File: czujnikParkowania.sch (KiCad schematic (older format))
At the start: 38 parts, among them J1 Screw_Terminal_01x03, Q1 BC817, Q2 IRF7404, Q3 BC817, Q4 BC817, Q5 BC817, U1 DC56-11SEKWA, U2 LM7805_TO220, U3 HC-SR04

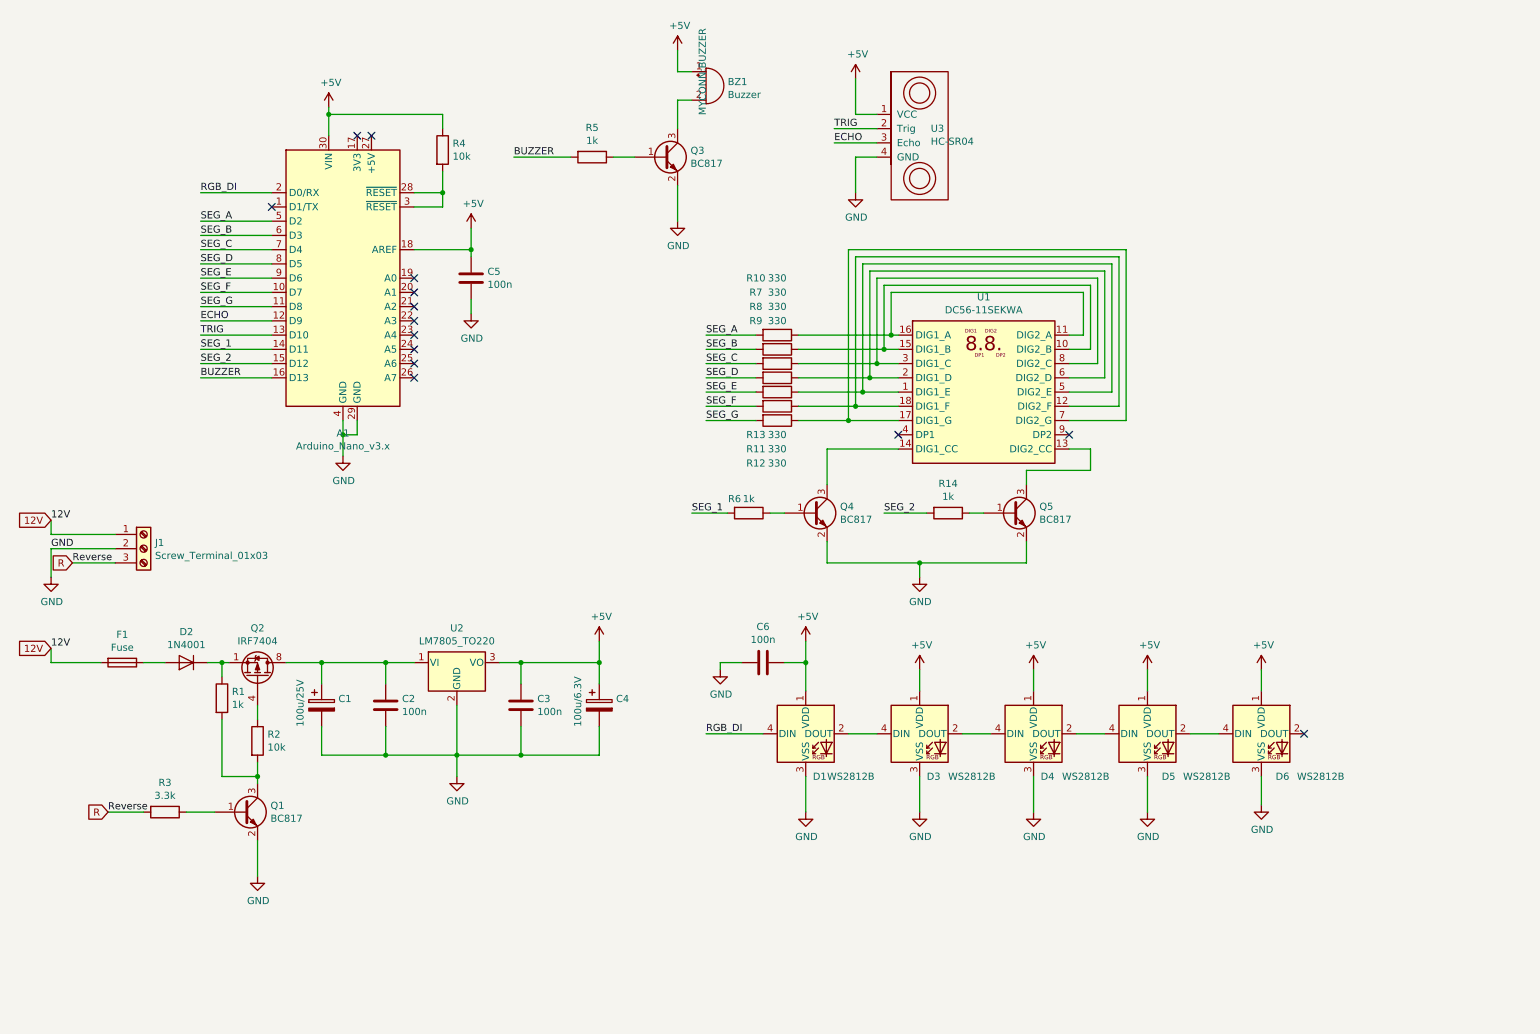
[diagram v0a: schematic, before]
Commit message: version with Amega only
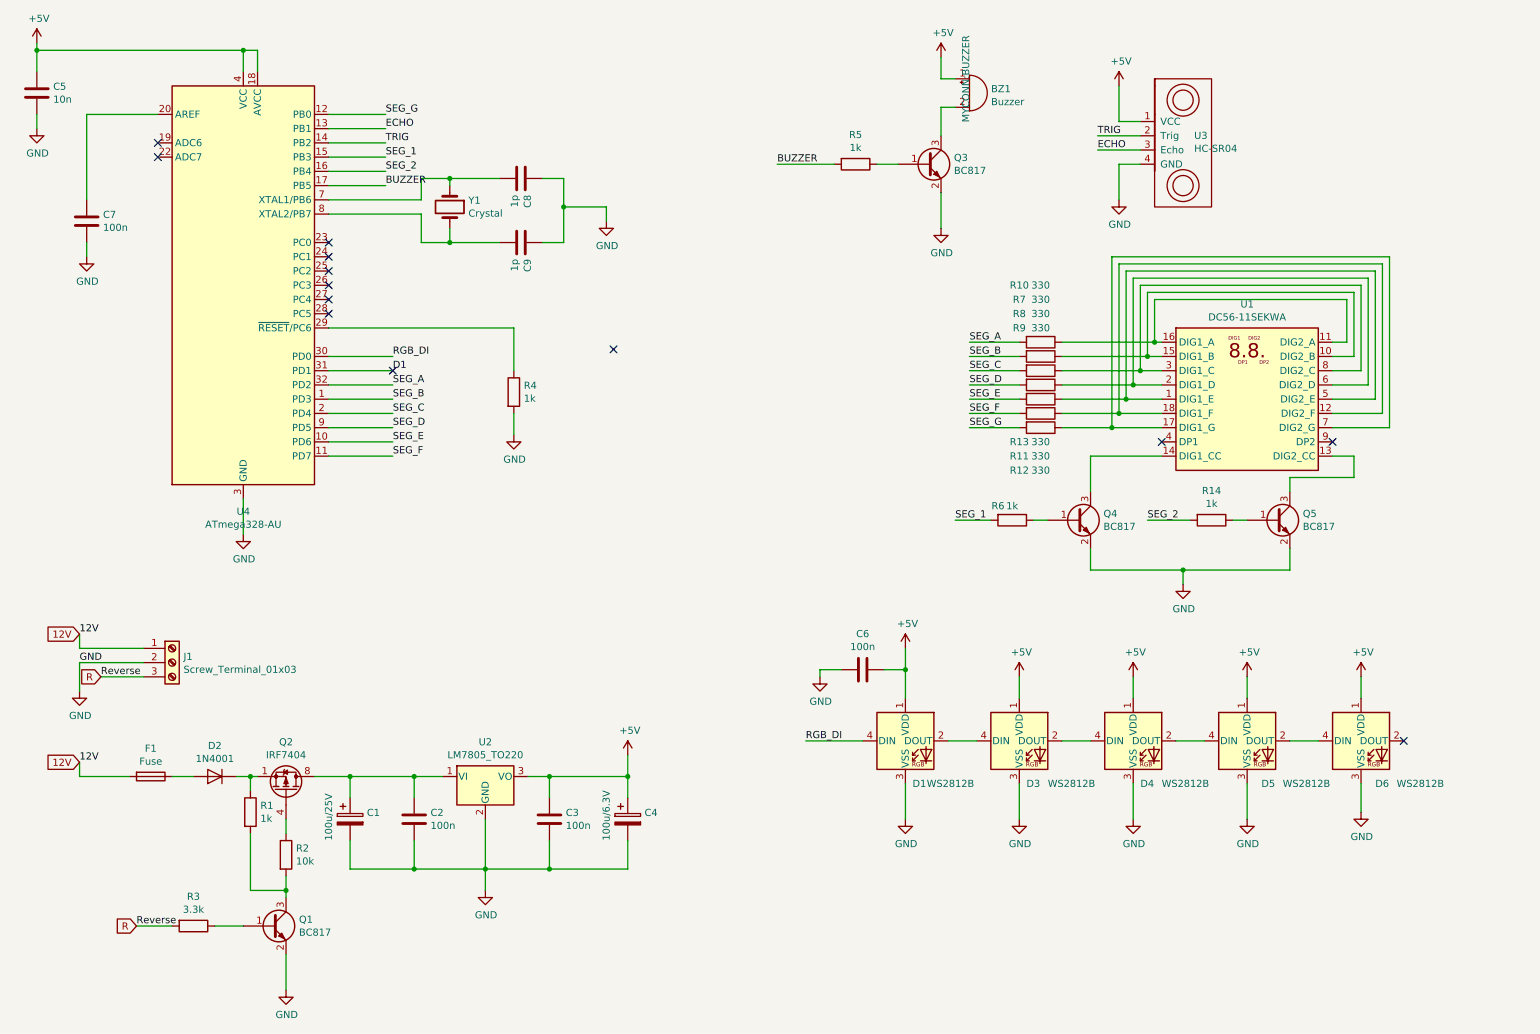
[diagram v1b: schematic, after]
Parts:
- removed A1: Arduino_Nano_v3.x, Module:Arduino_Nano, symbol MCU_Module:Arduino_Nano_v3.x
- added C7: 100n, Capacitor_SMD:C_0805_2012Metric, symbol Device:C
- added C8, C9: 1p, Capacitor_SMD:C_0805_2012Metric, symbol Device:C
- added U4: ATmega328-AU, Package_QFP:TQFP-32_7x7mm_P0.8mm, symbol MCU_Microchip_ATmega:ATmega328-AU
- added Y1: Crystal, MYCONN:16MHz cristal oscillator, symbol Device:Crystal
- C5: value 100n -> 10n
- R4: value 10k -> 1k
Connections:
- net +5V: now also U4.18 (AVCC), U4.4 (VCC), U4.6 (VCC); no longer R4.1
- net BUZZER: now also U4.17 (PB5)
- net ECHO: now also U4.13 (PB1)
- net GND: now also R4.2, C7.2, C8.1, C9.1, U4.21 (GND), U4.3 (GND), U4.5 (GND)
- net RGB_DI: now also U4.30 (PD0)
- net SEG_1: now also U4.15 (PB3)
- net SEG_2: now also U4.16 (PB4)
- net SEG_A: now also U4.32 (PD2)
- net SEG_B: now also U4.1 (PD3)
- net SEG_C: now also U4.2 (PD4)
- net SEG_D: now also U4.9 (PD5)
- net SEG_E: now also U4.10 (PD6)
- net SEG_F: now also U4.11 (PD7)
- net SEG_G: now also U4.12 (PB0)
- net TRIG: now also U4.14 (PB2)
- new net: C7.1, U4.20 (AREF)
- new net: R4.1, U4.29 (~RESET~/PC6)
- new net: C8.2, U4.7 (XTAL1/PB6), Y1.1
- new net: C9.2, U4.8 (XTAL2/PB7), Y1.2
- new net D1: U4.31 (PD1)
- no-connect marks 14 -> 13
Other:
- moved on the sheet: BZ1, C1, C2, C3, C4, C5, C6, D1, D2, D3, D4, D5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

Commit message: Adruino and Atmega328 on single board for code dev
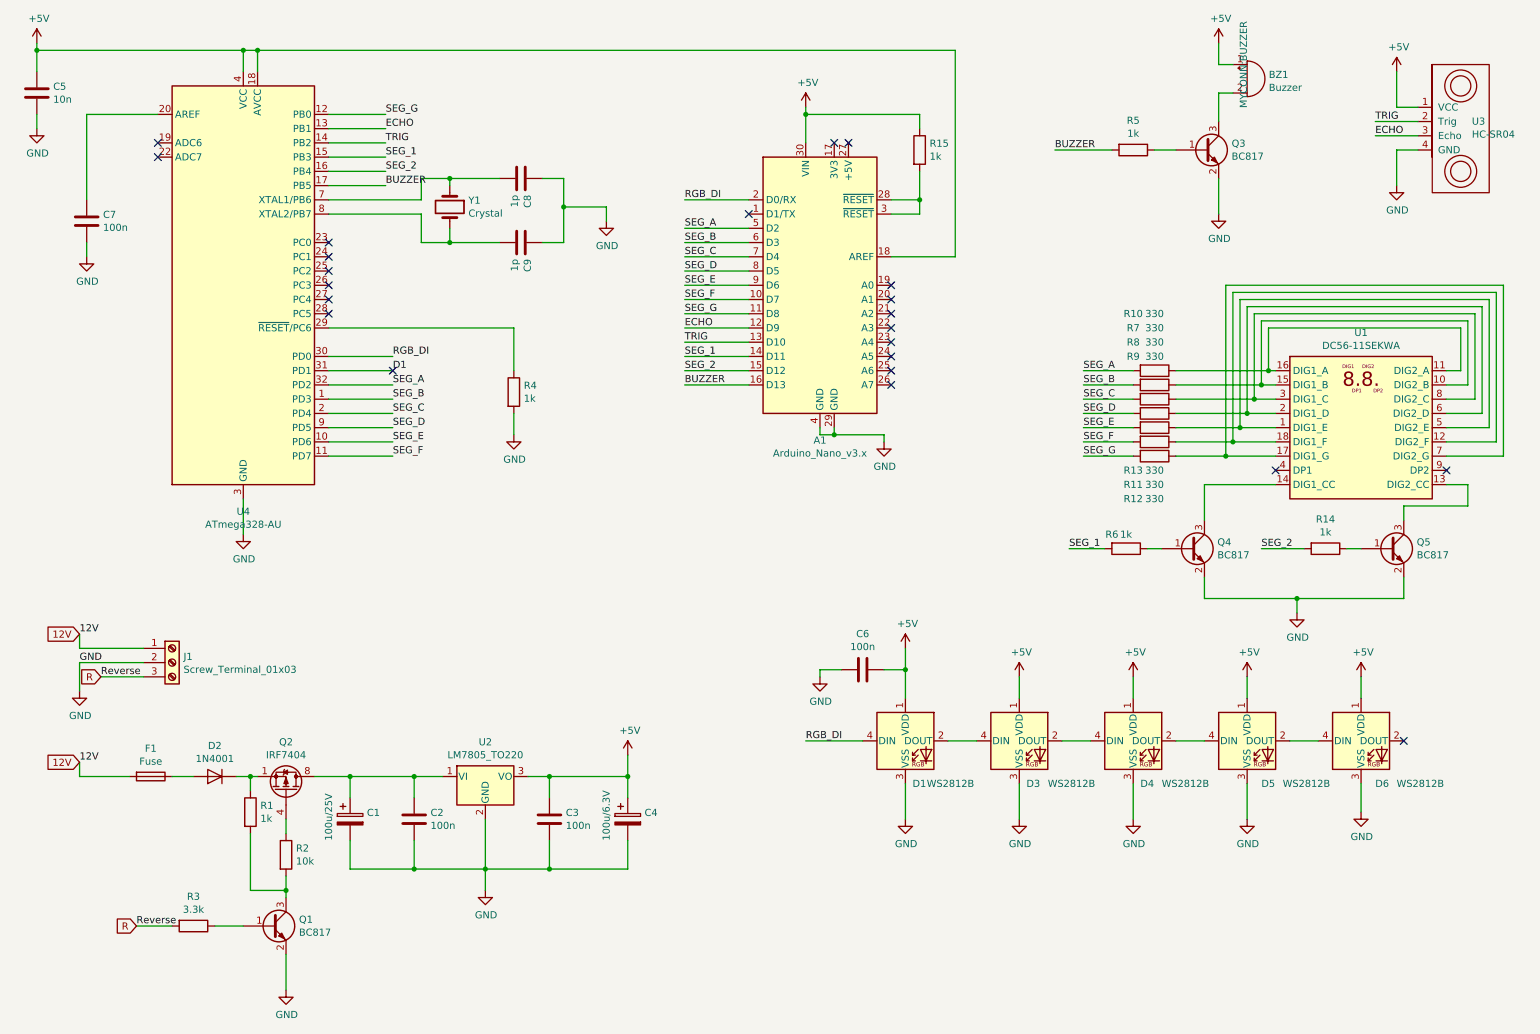
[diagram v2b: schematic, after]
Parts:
- added A1: Arduino_Nano_v3.x, Module:Arduino_Nano, symbol MCU_Module:Arduino_Nano_v3.x
- added R15: 1k, Resistor_SMD:R_0805_2012Metric, symbol Device:R
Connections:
- net +5V: now also A1.18 (AREF), A1.30 (VIN), R15.1
- net BUZZER: now also A1.16 (D13)
- net ECHO: now also A1.12 (D9)
- net GND: now also A1.29 (GND), A1.4 (GND)
- net RGB_DI: now also A1.2 (D0/RX)
- net SEG_1: now also A1.14 (D11)
- net SEG_2: now also A1.15 (D12)
- net SEG_A: now also A1.5 (D2)
- net SEG_B: now also A1.6 (D3)
- net SEG_C: now also A1.7 (D4)
- net SEG_D: now also A1.8 (D5)
- net SEG_E: now also A1.9 (D6)
- net SEG_F: now also A1.10 (D7)
- net SEG_G: now also A1.11 (D8)
- net TRIG: now also A1.13 (D10)
- new net: A1.28 (~RESET), A1.3 (~RESET), R15.2
- no-connect marks 13 -> 23
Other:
- moved on the sheet: BZ1, Q3, Q4, Q5, R10, R11, R12, R13, R14, R5, R6, R7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

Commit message: Added button
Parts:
- added SW?: SW_Push, symbol Switch:SW_Push
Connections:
- net D1 is gone; now on net BTN: U4.31 (PD1)
- net GND: now also SW?.2
- net BTN: now reaches A1.1 (D1/TX)
- net BTN: now also SW?.1
- no-connect marks 23 -> 21
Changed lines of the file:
@@
 RGB_DI
 Text Label 3150 3050 0    50   ~ 0
-D1
+BTN
 Text Label 3150 3150 0    50   ~ 0
 SEG_A
@@
 Text Label 3100 1750 0    50   ~ 0
 BUZZER
-NoConn ~ 3150 3050
 $Comp
 L MCU_Module:Arduino_Nano_v3.x A1
@@
 NoConn ~ 6650 3050
 NoConn ~ 6650 3150
-NoConn ~ 5650 1950
 $Comp
 L power:+5V #PWR0107
@@
 Text Label 5200 3150 0    50   ~ 0
 BUZZER
+$Comp
+L Switch:SW_Push SW?
+U 1 1 5EA69D05
+P 3700 4350
+F 0 "SW?" H 3700 4635 50  0000 C CNN
+F 1 "SW_Push" H 3700 4544 50  0000 C CNN
+F 2 "" H 3700 4550 50  0001 C CNN
+F 3 "~" H 3700 4550 50  0001 C CNN
+	1    3700 4350
+	1    0    0    -1
+$EndComp
+Wire Wire Line
+	5650 1950 5200 1950
+Text Label 5200 1950 0    50   ~ 0
+BTN
+Wire Wire Line
+	3500 4350 3150 4350
+$Comp
+L power:GND #PWR?
+U 1 1 5EAA1D9B
+P 4100 4450
+F 0 "#PWR?" H 4100 4200 50  0001 C CNN
+F 1 "GND" H 4105 4277 50  0000 C CNN
+F 2 "" H 4100 4450 50  0001 C CNN
+F 3 "" H 4100 4450 50  0001 C CNN
+	1    4100 4450
+	1    0    0    -1
+$EndComp
+Wire Wire Line
+	3900 4350 4100 4350
+Wire Wire Line
+	4100 4350 4100 4450
+Text Label 3150 4350 0    50   ~ 0
+BTN
 $EndSCHEMATC

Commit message: bug on schematic and missing connection on PCB
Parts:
- SW1: renamed from SW?; footprint (none) -> Button_Switch_SMD:SW_SPST_B3S-1000
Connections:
- net +5V: no longer A1.18 (AREF)
- net at C7.1, U4.20 (AREF): now also A1.18 (AREF)
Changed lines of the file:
@@
 	6650 2250 7100 2250
-Wire Wire Line
-	7100 2250 7100 800
-Wire Wire Line
-	7100 800  2200 800
-Connection ~ 2200 800
 Wire Wire Line
 	5650 1850 5200 1850
@@
 BUZZER
 $Comp
-L Switch:SW_Push SW?
+L Switch:SW_Push SW1
 U 1 1 5EA69D05
 P 3700 4350
-F 0 "SW?" H 3700 4635 50  0000 C CNN
+F 0 "SW1" H 3700 4635 50  0000 C CNN
 F 1 "SW_Push" H 3700 4544 50  0000 C CNN
-F 2 "" H 3700 4550 50  0001 C CNN
-F 3 "~" H 3700 4550 50  0001 C CNN
+F 2 "Button_Switch_SMD:SW_SPST_B3S-1000" H 3700 4550 50  0001 C CNN
+F 3 "https://www.tme.eu/pl/details/b3s-1000/mikroprzelaczniki-tact/omron-ocb/" H 3700 4550 50  0001 C CNN
 	1    3700 4350
 	1    0    0    -1
@@
 	3500 4350 3150 4350
 $Comp
-L power:GND #PWR?
+L power:GND #PWR0129
 U 1 1 5EAA1D9B
 P 4100 4450
-F 0 "#PWR?" H 4100 4200 50  0001 C CNN
+F 0 "#PWR0129" H 4100 4200 50  0001 C CNN
 F 1 "GND" H 4105 4277 50  0000 C CNN
 F 2 "" H 4100 4450 50  0001 C CNN
@@
 Text Label 3150 4350 0    50   ~ 0
 BTN
+Wire Wire Line
+	7100 650  1000 650
+Wire Wire Line
+	1000 650  1000 1250
+Wire Wire Line
+	7100 650  7100 2250
+Connection ~ 1000 1250
 $EndSCHEMATC

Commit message: added capacitors
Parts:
- added C10, C11, C12, C13: 100n, Capacitor_SMD:C_0805_2012Metric, symbol Device:C
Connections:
- net +5V: now also C10.1, C11.1, C12.1, C13.1
- net GND: now also C10.2, C11.2, C12.2, C13.2
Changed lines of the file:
@@
 L power:+5V #PWR0121
 U 1 1 5EB28EBD
-P 7550 5200
-F 0 "#PWR0121" H 7550 5050 50  0001 C CNN
-F 1 "+5V" H 7565 5373 50  0000 C CNN
-F 2 "" H 7550 5200 50  0001 C CNN
-F 3 "" H 7550 5200 50  0001 C CNN
-	1    7550 5200
+P 7550 5000
+F 0 "#PWR0121" H 7550 4850 50  0001 C CNN
+F 1 "+5V" H 7565 5173 50  0000 C CNN
+F 2 "" H 7550 5000 50  0001 C CNN
+F 3 "" H 7550 5000 50  0001 C CNN
+	1    7550 5000
 	1    0    0    -1
 $EndComp
@@
 L power:+5V #PWR0122
 U 1 1 5EB296B5
-P 8350 5200
-F 0 "#PWR0122" H 8350 5050 50  0001 C CNN
-F 1 "+5V" H 8365 5373 50  0000 C CNN
-F 2 "" H 8350 5200 50  0001 C CNN
-F 3 "" H 8350 5200 50  0001 C CNN
-	1    8350 5200
+P 8350 5000
+F 0 "#PWR0122" H 8350 4850 50  0001 C CNN
+F 1 "+5V" H 8365 5173 50  0000 C CNN
+F 2 "" H 8350 5000 50  0001 C CNN
+F 3 "" H 8350 5000 50  0001 C CNN
+	1    8350 5000
 	1    0    0    -1
 $EndComp
@@
 L power:+5V #PWR0123
 U 1 1 5EB2995A
-P 9150 5200
-F 0 "#PWR0123" H 9150 5050 50  0001 C CNN
-F 1 "+5V" H 9165 5373 50  0000 C CNN
-F 2 "" H 9150 5200 50  0001 C CNN
-F 3 "" H 9150 5200 50  0001 C CNN
-	1    9150 5200
+P 9150 5000
+F 0 "#PWR0123" H 9150 4850 50  0001 C CNN
+F 1 "+5V" H 9165 5173 50  0000 C CNN
+F 2 "" H 9150 5000 50  0001 C CNN
+F 3 "" H 9150 5000 50  0001 C CNN
+	1    9150 5000
 	1    0    0    -1
 $EndComp
@@
 L power:+5V #PWR0124
 U 1 1 5EB29CCE
-P 9950 5200
-F 0 "#PWR0124" H 9950 5050 50  0001 C CNN
-F 1 "+5V" H 9965 5373 50  0000 C CNN
-F 2 "" H 9950 5200 50  0001 C CNN
-F 3 "" H 9950 5200 50  0001 C CNN
-	1    9950 5200
-	1    0    0    -1
-$EndComp
-Wire Wire Line
-	7550 5200 7550 5350
-Wire Wire Line
-	8350 5200 8350 5350
-Wire Wire Line
-	9150 5200 9150 5350
-Wire Wire Line
-	9950 5200 9950 5350
+P 9950 5000
+F 0 "#PWR0124" H 9950 4850 50  0001 C CNN
+F 1 "+5V" H 9965 5173 50  0000 C CNN
+F 2 "" H 9950 5000 50  0001 C CNN
+F 3 "" H 9950 5000 50  0001 C CNN
+	1    9950 5000
+	1    0    0    -1
+$EndComp
 Wire Wire Line
 	7050 5650 7250 5650
@@
 	7100 650  7100 2250
 Connection ~ 1000 1250
+Wire Wire Line
+	9950 5000 9950 5150
+Wire Wire Line
+	9150 5000 9150 5150
+Wire Wire Line
+	8350 5000 8350 5150
+Wire Wire Line
+	7550 5000 7550 5150
+$Comp
+L Device:C C10
+U 1 1 5EC7958F
+P 7250 5150
+F 0 "C10" V 6998 5150 50  0000 C CNN
+F 1 "100n" V 7089 5150 50  0000 C CNN
+F 2 "Capacitor_SMD:C_0805_2012Metric" H 7288 5000 50  0001 C CNN
+F 3 "~" H 7250 5150 50  0001 C CNN
+	1    7250 5150
+	0    1    1    0
+$EndComp
+$Comp
+L Device:C C11
+U 1 1 5EC79A1F
+P 8050 5150
+F 0 "C11" V 7798 5150 50  0000 C CNN
+F 1 "100n" V 7889 5150 50  0000 C CNN
+F 2 "Capacitor_SMD:C_0805_2012Metric" H 8088 5000 50  0001 C CNN
+F 3 "~" H 8050 5150 50  0001 C CNN
+	1    8050 5150
+	0    1    1    0
+$EndComp
+$Comp
+L Device:C C12
+U 1 1 5EC79EB5
+P 8850 5150
+F 0 "C12" V 8598 5150 50  0000 C CNN
+F 1 "100n" V 8689 5150 50  0000 C CNN
+F 2 "Capacitor_SMD:C_0805_2012Metric" H 8888 5000 50  0001 C CNN
+F 3 "~" H 8850 5150 50  0001 C CNN
+	1    8850 5150
+	0    1    1    0
+$EndComp
+$Comp
+L Device:C C13
+U 1 1 5EC7A1D8
+P 9700 5150
+F 0 "C13" V 9448 5150 50  0000 C CNN
+F 1 "100n" V 9539 5150 50  0000 C CNN
+F 2 "Capacitor_SMD:C_0805_2012Metric" H 9738 5000 50  0001 C CNN
+F 3 "~" H 9700 5150 50  0001 C CNN
+	1    9700 5150
+	0    1    1    0
+$EndComp
+$Comp
+L power:GND #PWR0130
+U 1 1 5EC7A618
+P 7000 5200
+F 0 "#PWR0130" H 7000 4950 50  0001 C CNN
+F 1 "GND" H 7005 5027 50  0000 C CNN
+F 2 "" H 7000 5200 50  0001 C CNN
+F 3 "" H 7000 5200 50  0001 C CNN
+	1    7000 5200
+	1    0    0    -1
+$EndComp
+$Comp
+L power:GND #PWR0131
+U 1 1 5EC7A8EC
+P 7800 5200
+F 0 "#PWR0131" H 7800 4950 50  0001 C CNN
+F 1 "GND" H 7805 5027 50  0000 C CNN
+F 2 "" H 7800 5200 50  0001 C CNN
+F 3 "" H 7800 5200 50  0001 C CNN
+	1    7800 5200
+	1    0    0    -1
+$EndComp
+$Comp
+L power:GND #PWR0132
+U 1 1 5EC7ABA1
+P 8600 5200
+F 0 "#PWR0132" H 8600 4950 50  0001 C CNN
+F 1 "GND" H 8605 5027 50  0000 C CNN
+F 2 "" H 8600 5200 50  0001 C CNN
+F 3 "" H 8600 5200 50  0001 C CNN
+	1    8600 5200
+	1    0    0    -1
+$EndComp
+$Comp
+L power:GND #PWR0133
+U 1 1 5EC7ADED
+P 9450 5200
+F 0 "#PWR0133" H 9450 4950 50  0001 C CNN
+F 1 "GND" H 9455 5027 50  0000 C CNN
+F 2 "" H 9450 5200 50  0001 C CNN
+F 3 "" H 9450 5200 50  0001 C CNN
+	1    9450 5200
+	1    0    0    -1
+$EndComp
+Wire Wire Line
+	9850 5150 9950 5150
+Connection ~ 9950 5150
+Wire Wire Line
+	9950 5150 9950 5350
+Wire Wire Line
+	9550 5150 9450 5150
+Wire Wire Line
+	9450 5150 9450 5200
+Wire Wire Line
+	9000 5150 9150 5150
+Connection ~ 9150 5150
+Wire Wire Line
+	9150 5150 9150 5350
+Wire Wire Line
+	8700 5150 8600 5150
+Wire Wire Line
+	8600 5150 8600 5200
+Wire Wire Line
+	8200 5150 8350 5150
+Connection ~ 8350 5150
+Wire Wire Line
+	8350 5150 8350 5350
+Wire Wire Line
+	7900 5150 7800 5150
+Wire Wire Line
+	7800 5150 7800 5200
+Wire Wire Line
+	7400 5150 7550 5150
+Connection ~ 7550 5150
+Wire Wire Line
+	7550 5150 7550 5350
+Wire Wire Line
+	7100 5150 7000 5150
+Wire Wire Line
+	7000 5150 7000 5200
 $EndSCHEMATC

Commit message: schematic reset pin bug fix
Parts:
- R4: value 1k -> 10k
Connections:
- net +5V: now also R4.1
- net GND: no longer R4.2
- net at U4.29 (~RESET~/PC6): now also R4.2; no longer R4.1
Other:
- moved on the sheet: R4
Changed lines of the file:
@@
 F 1 "IRF7404" V 2651 6000 50  0000 C CNN
 F 2 "Package_SO:SOIC-8_3.9x4.9mm_P1.27mm" H 2600 5925 50  0001 L CIN
-F 3 "http://www.infineon.com/dgdl/irf7404.pdf?fileId=5546d462533600a4015355fa2b5b1b9e" V 2400 6000 50  0001 L CNN
+F 3 "https://www.tme.eu/pl/details/ao4441/tranzystory-z-kanalem-p-smd/alpha-omega-semiconductor/" V 2400 6000 50  0001 L CNN
 	1    2400 6000
 	0    1    -1   0
@@
 Wire Wire Line
 	2700 3650 3150 3650
-Wire Wire Line
-	2700 2750 4000 2750
-$Comp
-L power:GND #PWR0127
-U 1 1 5EBE9E5B
-P 4000 3500
-F 0 "#PWR0127" H 4000 3250 50  0001 C CNN
-F 1 "GND" H 4005 3327 50  0000 C CNN
-F 2 "" H 4000 3500 50  0001 C CNN
-F 3 "" H 4000 3500 50  0001 C CNN
-	1    4000 3500
-	1    0    0    -1
-$EndComp
 $Comp
 L Device:R R4
 U 1 1 5EBEA221
-P 4000 3200
-F 0 "R4" H 4070 3246 50  0000 L CNN
-F 1 "1k" H 4070 3155 50  0000 L CNN
-F 2 "Resistor_SMD:R_0805_2012Metric" V 3930 3200 50  0001 C CNN
-F 3 "~" H 4000 3200 50  0001 C CNN
-	1    4000 3200
-	1    0    0    -1
-$EndComp
-Wire Wire Line
-	4000 2750 4000 3050
-Wire Wire Line
-	4000 3350 4000 3500
+P 3050 2450
+F 0 "R4" H 3120 2496 50  0000 L CNN
+F 1 "10k" H 3120 2405 50  0000 L CNN
+F 2 "Resistor_SMD:R_0805_2012Metric" V 2980 2450 50  0001 C CNN
+F 3 "~" H 3050 2450 50  0001 C CNN
+	1    3050 2450
+	1    0    0    -1
+$EndComp
 NoConn ~ 1500 1450
 NoConn ~ 1500 1550
@@
 Wire Wire Line
 	7000 5150 7000 5200
+$Comp
+L power:+5V #PWR?
+U 1 1 5EB19907
+P 3050 2200
+F 0 "#PWR?" H 3050 2050 50  0001 C CNN
+F 1 "+5V" H 3065 2373 50  0000 C CNN
+F 2 "" H 3050 2200 50  0001 C CNN
+F 3 "" H 3050 2200 50  0001 C CNN
+	1    3050 2200
+	1    0    0    -1
+$EndComp
+Wire Wire Line
+	3050 2200 3050 2300
+Wire Wire Line
+	3050 2600 3050 2750
+Wire Wire Line
+	3050 2750 2700 2750
 $EndSCHEMATC
